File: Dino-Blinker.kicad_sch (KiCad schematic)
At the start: 26 parts, among them IC1 M74HC4060YRM13TR, J1 Conn_01x02_Pin

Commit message: added QR
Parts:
- J1: footprint Connector_Wago:Wago_734-132_1x02_P3.50mm_Vertical -> Connector_PinHeader_2.54mm:PinHeader_1x02_P2.54mm_Vertical

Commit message: added folder Pics
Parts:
- IC1: footprint SamacSys_Parts:SOIC127P600X175-16N -> Package_SO:SOIC-16_3.9x9.9mm_P1.27mm
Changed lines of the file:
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@@
 			)
 		)
-		(property "Footprint" "SamacSys_Parts:SOIC127P600X175-16N"
+		(property "Footprint" "Package_SO:SOIC-16_3.9x9.9mm_P1.27mm"
 			(at 224.155 184.455 0)
 			(effects

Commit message: run kibot
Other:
- moved on the sheet: C1, C2, D10, D3, D4, D6, D7, D8, D9, IC1, J1, R10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

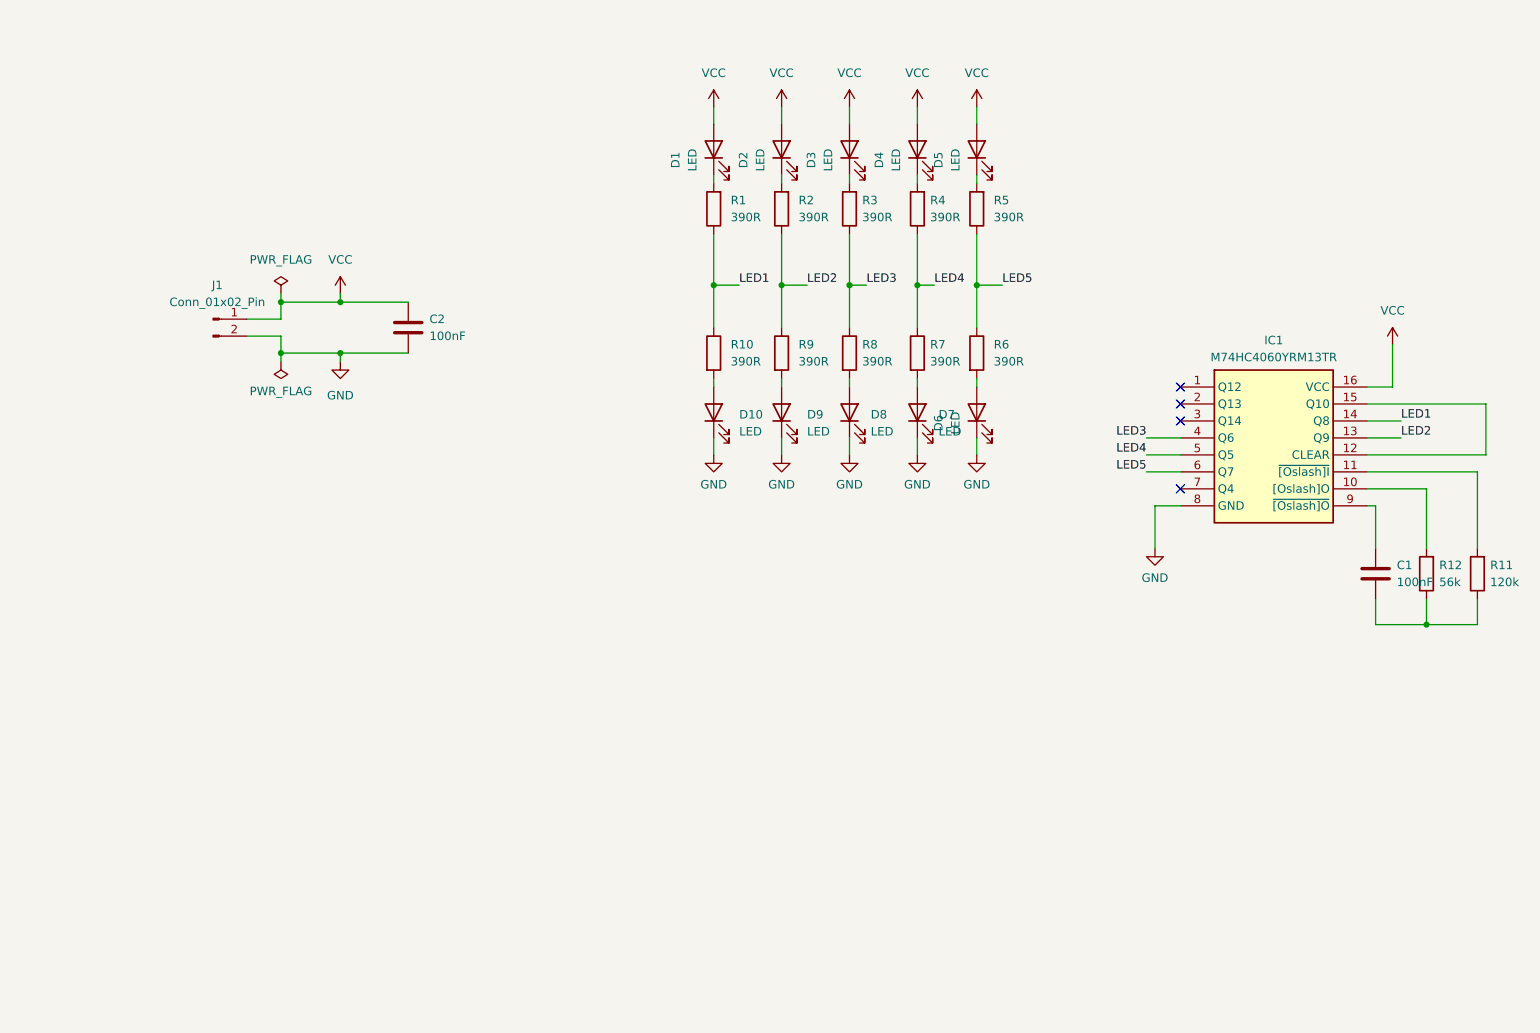
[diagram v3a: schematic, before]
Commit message: 0402er Leds
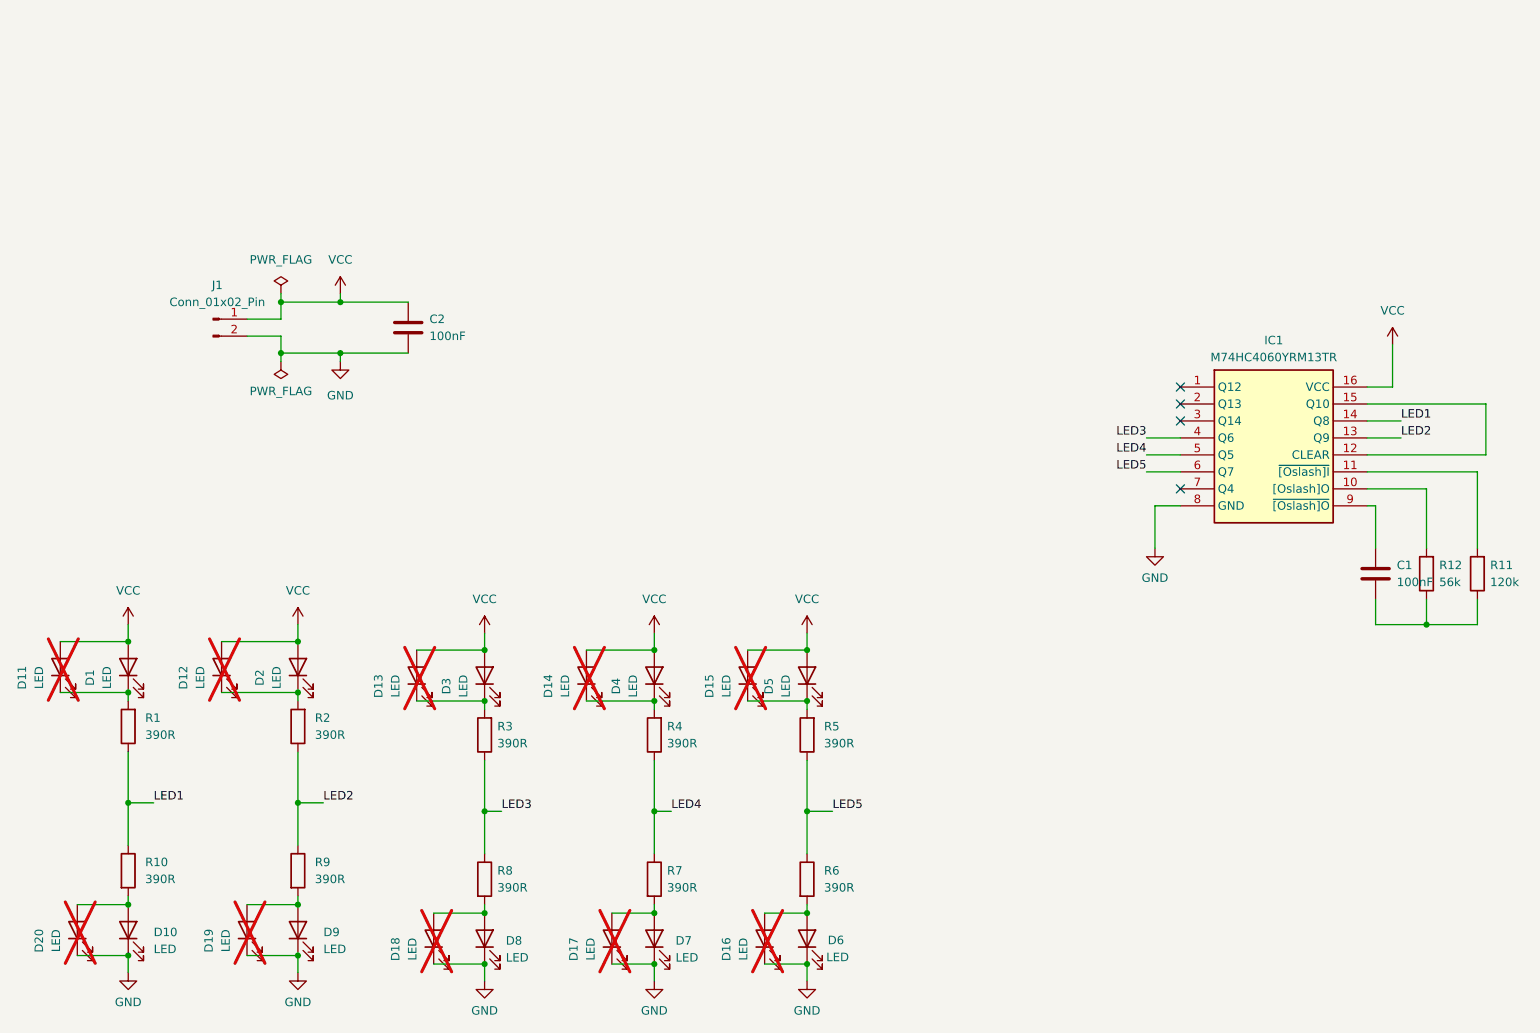
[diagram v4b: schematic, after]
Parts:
- added D11, D12, D13, D14, D15, D16, D17, D18, D19, D20: LED, LED_SMD:LED_0402_1005Metric_Pad0.77x0.64mm_HandSolder, symbol Device:LED
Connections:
- net GND: now also D16.1 (K), D17.1 (K), D18.1 (K), D19.1 (K), D20.1 (K)
- net VCC: now also D11.2 (A), D12.2 (A), D13.2 (A), D14.2 (A), D15.2 (A)
- net at D9.2 (A), R9.2: now also D19.2 (A)
- net at D4.1 (K), R4.2: now also D14.1 (K)
- net at D7.2 (A), R7.2: now also D17.2 (A)
- net at D6.2 (A), R6.2: now also D16.2 (A)
- net at D2.1 (K), R2.2: now also D12.1 (K)
- net at D1.1 (K), R1.2: now also D11.1 (K)
- net at D5.1 (K), R5.2: now also D15.1 (K)
- net at D3.1 (K), R3.2: now also D13.1 (K)
- net at D10.2 (A), R10.2: now also D20.2 (A)
- net at D8.2 (A), R8.2: now also D18.2 (A)
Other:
- moved on the sheet: D1, D10, D2, D3, D4, D5, D6, D7, D8, D9, R1, R10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
